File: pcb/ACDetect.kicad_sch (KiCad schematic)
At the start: 5 parts, among them U1 HCPL-3700M

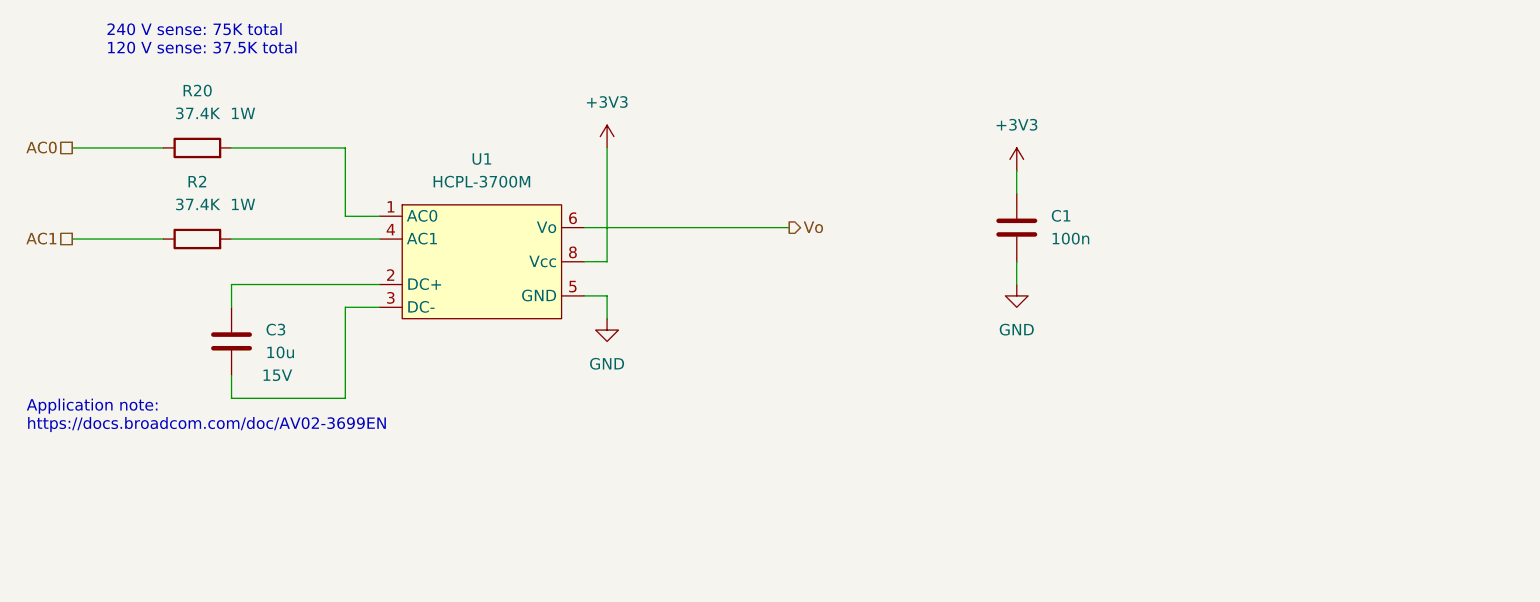
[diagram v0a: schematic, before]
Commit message: Swap 1Wire and AC sense
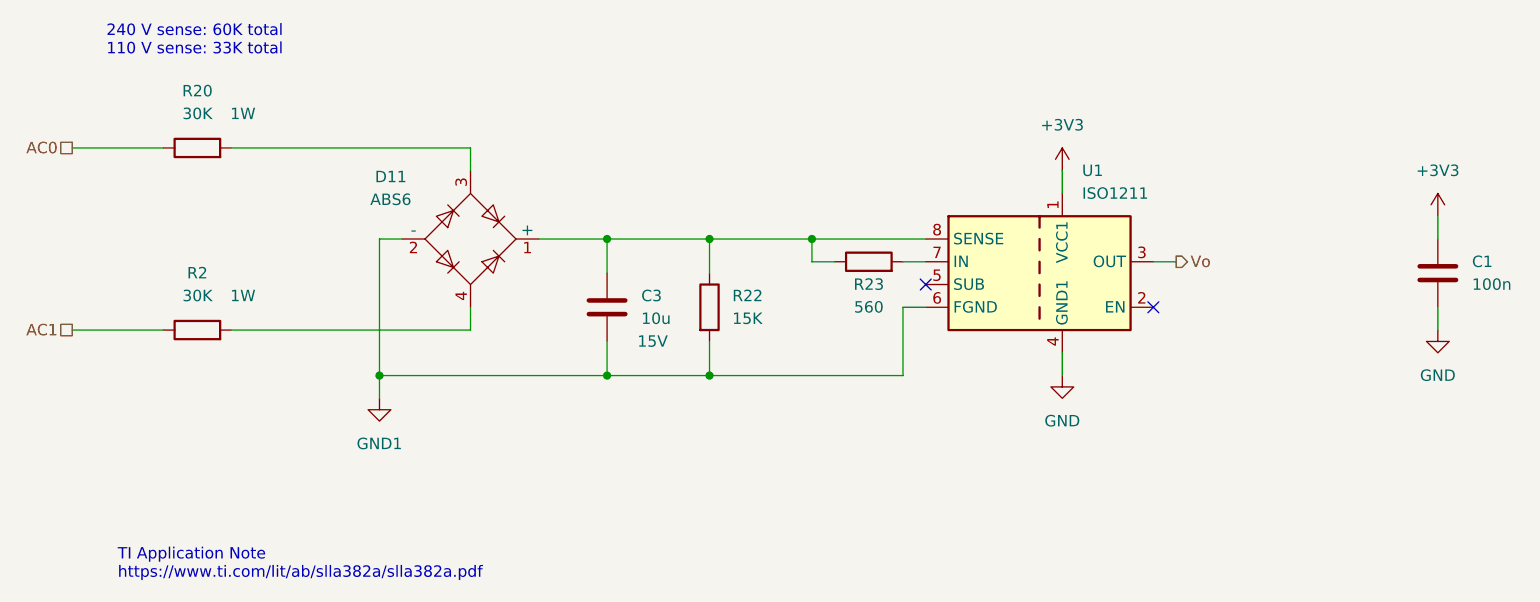
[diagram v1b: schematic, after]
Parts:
- removed U1: HCPL-3700M, Package_DIP:SMDIP-8_W7.62mm, symbol hcpl3700m:HCPL-3700M
- added D11: ABS6, Diode_SMD:Diode_Bridge_Diotec_ABS, symbol Diode_Bridge:ABS6
- added R22: 15K, Resistor_SMD:R_0603_1608Metric, symbol Device:R
- added R23: 560, Resistor_SMD:R_0603_1608Metric, symbol Device:R
- added U1: ISO1211, Package_SO:SOIC-8_3.9x4.9mm_P1.27mm, symbol Isolator:ISO1211
- C1: LCSC (none) -> C1525
- R2, R20: value 37.4K -> 30K; MPN CRCW251237K4FKTH -> CRCW251230K0JNEG
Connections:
- net +3V3: now also U1.1 (VCC1)
- net GND: now also U1.4 (GND1)
- net Vo: now also U1.3 (OUT)
- net at R2.2: now also D11.4
- net at R20.2: now also D11.3
- net at C3.1: now also D11.1 (+), R22.1, R23.1, U1.8 (SENSE)
- net GND1: now reaches C3.2
- net GND1: now also D11.2 (-), R22.2, U1.6 (FGND)
- new net: R23.2, U1.7 (IN)
- no-connect marks 0 -> 2
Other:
- note added: "240 V sense: 60K total 110 V sense: 33K total"
- note added: "TI Application Note https://www.ti.com/lit/ab/slla382a/slla382a.pdf"
- note removed: "240 V sense: 75K total 120 V sense: 37.5K total"
- note removed: "Application note: https://docs.broadcom.com/doc/AV02-3699EN"
- moved on the sheet: C1, C3, R2
